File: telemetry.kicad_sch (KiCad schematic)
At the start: 52 parts, among them J1 DT13-08PA, J10 Conn_01x02, J11 Conn_01x03, J12 Conn_01x03, J13 Conn_01x03, J14 Conn_01x06, J2 Conn_01x02, J3 Conn_01x06, J4 Conn_01x06, J5 Conn_01x06, J6 Conn_01x06, J7 Conn_01x06, J8 Conn_01x06, J9 Micro_SD_Card, Q1 BS170F, Q2 BS170F, U1 RP2350_Plus, U2 MCP2517FD-xSL, U3 TLV76133DCY, U4 DS1307+, U5 R-78C5.0-1.0, U6 MCP2551-I-P, Y2 ABS07-32.768KHZ-T

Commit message: Complete (hopefully) schematic
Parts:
- removed U1: RP2350_Plus, symbol Telemetry:RP2350_Plus
- removed U2: MCP2517FD-xSL, Package_SO:SOIC-14_3.9x8.7mm_P1.27mm, symbol Interface_CAN_LIN:MCP2517FD-xSL
- added C12, C13, C14, C8, C9: 10n, Capacitor_SMD:C_0805_2012Metric, symbol Device:C_Small
- added J15, J16, J17, J18, J19: Conn_01x03, Connector_JST:JST_XA_B03B-XASK-1_1x03_P2.50mm_Vertical, symbol Connector_Generic:Conn_01x03
- added R10, R11, R12, R13, R6: 100, Resistor_SMD:R_0805_2012Metric, symbol Device:R_Small
- added U2: Waveshare ESP32-S3 Devboard, symbol Telemetry:Waveshare_ESP-S3
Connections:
- net A0_GND is gone; now on net GND: C10.2, C11.2, C5.2, J11.3 (Pin_3), J12.3 (Pin_3), J13.3 (Pin_3)
- net +3V3: now also J15.1 (Pin_1), J16.1 (Pin_1), J17.1 (Pin_1), J18.1 (Pin_1), J19.1 (Pin_1)
- net +5V: now also U2.2 (5V)
- net A0: now also U2.19 (GPIO4)
- net A0_SIG: now also J16.2 (Pin_2); no longer J13.2 (Pin_2)
- net A1: now also U2.18 (GPIO5)
- net A1_SIG: now also J17.2 (Pin_2); no longer J11.2 (Pin_2)
- net A2: now also U2.17 (GPIO6)
- net A2_SIG: now also J18.2 (Pin_2); no longer J12.2 (Pin_2)
- net GND: now also C12.2, C13.2, C14.2, C8.2, C9.2, J15.3 (Pin_3), J16.3 (Pin_3), J17.3 (Pin_3), J18.3 (Pin_3), J19.3 (Pin_3), U2.1 (GND), U2.23 (GND), U2.43 (GND), U2.44 (GND)
- net GPS(SCL/RX): now also U2.28 (GPIO42)
- net GPS(SDA/TX): now also U2.29 (GPIO41)
- net I2C0_0_GPIO: now also U2.9 (GPIO46)
- net I2C0_1_GPIO: now also U2.10 (GPIO3)
- net I2C0_SCL: now also U2.27 (GPIO2)
- net I2C0_SDA: now also U2.35 (GPIO35)
- net I2C1_0_GPIO: now also U2.37 (GPIO45)
- net I2C1_1_GPIO: now also U2.36 (GPIO0)
- net SD_CS: now also U2.8 (GPIO9)
- net SD_MISO: now also U2.12 (GPIO18)
- net SD_MOSI: now also U2.11 (GPIO8)
- net SD_SCK: now also U2.13 (GPIO17)
- net SPI1_0_CS: now also U2.32 (GPIO38)
- net SPI1_1_CS: now also U2.7 (GPIO10)
- net SPI1_MISO: now also U2.30 (GPIO40)
- net SPI1_MOSI: now also U2.33 (GPIO37)
- net SPI1_SCK: now also U2.31 (GPIO39)
- net W0: now also U2.40 (GPIO21)
- net W1: now also U2.39 (GPIO47)
- net W2: now also U2.26 (GPIO1)
- net W3: now also U2.38 (GPIO48)
- net CANRX renamed CAN_RX
- net CAN_RX: now also U2.14 (GPIO16)
- net CANTX renamed CAN_TX
- net CAN_TX: now also U2.15 (GPIO15)
- new net A3: C8.1, R6.1, U2.16 (GPIO7)
- new net A3_SIG: J19.2 (Pin_2), R6.2
- new net A4: C9.1, R10.1
- new net A4_SIG: J15.2 (Pin_2), R10.2
- new net A5: C12.1, R11.1, U2.6 (GPIO11)
- new net A5_SIG: J13.2 (Pin_2), R11.2
- new net A6: C13.1, R12.1, U2.5 (GPIO12)
- new net A6_SIG: J11.2 (Pin_2), R12.2
- new net A7: C14.1, R13.1, U2.4 (GPIO13)
- new net A7_SIG: J12.2 (Pin_2), R13.2
- new net A8: U2.3 (GPIO14)
- no-connect marks 8 -> 12
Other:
- note added: "Analogue Input Connectors"
- note added: "CAN Transeiver"
- note added: "GPS I2C/UART Connector"
- note removed: "CAN"
- note removed: "Digital Input Connectors"
- moved on the sheet: BT1, C10, C11, C5, H1, H2, H3, H4, J11, J12, J13, J14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

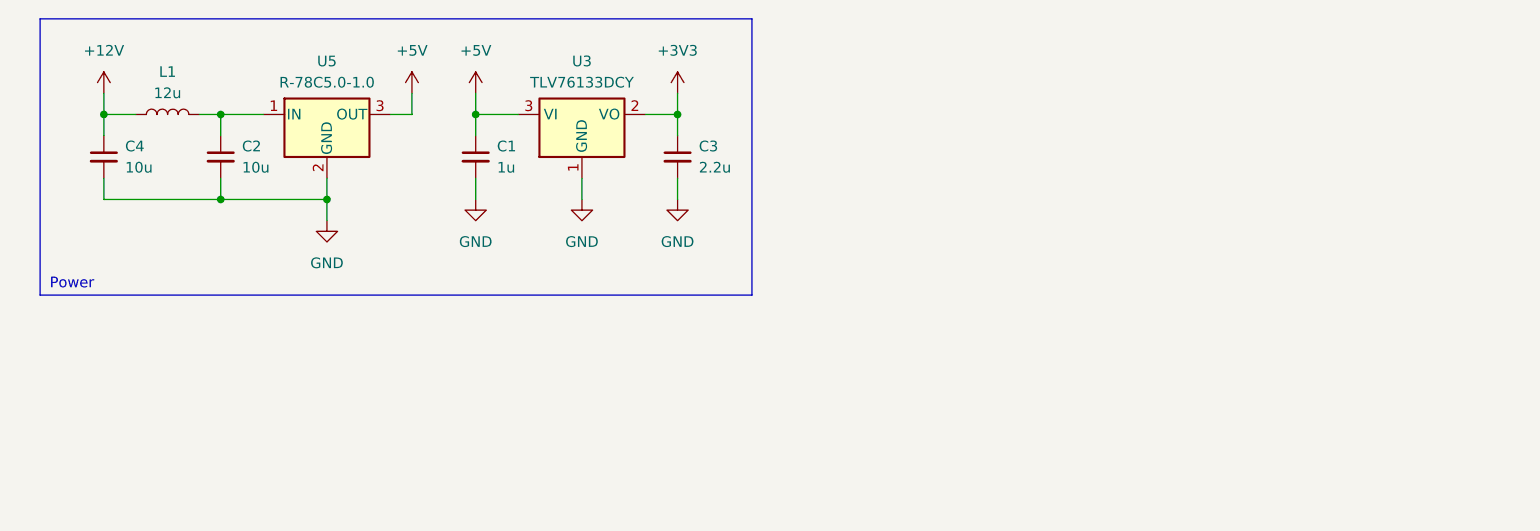
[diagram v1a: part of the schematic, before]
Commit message: added ESP32, connector footprint
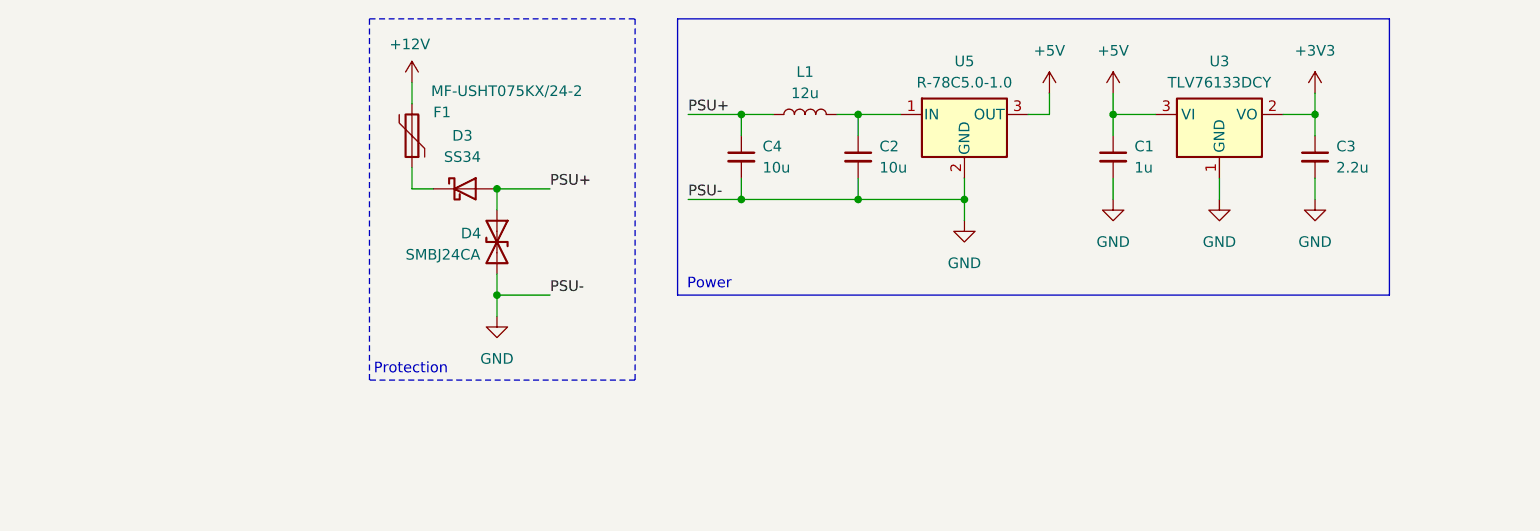
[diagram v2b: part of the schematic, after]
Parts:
- added D3: SS34, Diode_SMD:D_SMA, symbol Diode:SS34
- added D4: SMBJ24CA, Diode_SMD:D_SMB, symbol Device:D_TVS
- added F1: MF-USHT075KX/24-2, Inductor_SMD:L_1210_3225Metric, symbol Device:Polyfuse
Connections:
- net +12V: now also F1.2; no longer C4.1, L1.1
- net GND: now also D4.2 (A2)
- new net: D3.1 (K), F1.1
- new net PSU+: C4.1, D3.2 (A), D4.1 (A1), L1.1
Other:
- note added: "Protection"
- moved on the sheet: C1, C2, C3, C4, L1, U3, U5

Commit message: Place and route important components
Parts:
- removed J1: DT13-08PA, Connector_DT:TE_DT13-08PA, symbol Connector_Generic:Conn_02x04_Counter_Clockwise
- added J1, J22: Conn_01x02, Connector_JST:JST_XA_B02B-XASK-1_1x02_P2.50mm_Vertical, symbol Connector_Generic:Conn_01x02
- added J20, J21: DT13-2P, Connector_DT:TE_DT13-2P, symbol Connector_Generic:Conn_01x02
- C1, C3: footprint (none) -> Capacitor_SMD:C_0805_2012Metric
- J10, J2: value Conn_01x02 -> DT13-2P; footprint (none) -> Connector_DT:TE_DT13-2P
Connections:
- net GND: now also J1.2 (Pin_2), J20.2 (Pin_2), J21.2 (Pin_2), J22.2 (Pin_2)
- net W0: now also J1.1 (Pin_1)
- net W1: now also J22.1 (Pin_1)
- net W2: now also J20.1 (Pin_1)
- net W3: now also J21.1 (Pin_1)
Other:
- note added: "Front Wheel Speed Sensors"
- note added: "Power Supply"
- note added: "Rear Wheel Speed Sensors"
- note removed: "Power"
- note removed: "Wheel Speed Sensors Connector"
- moved on the sheet: C1, C2, C3, C4, D3, D4, F1, H1, H2, H3, H4, J10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

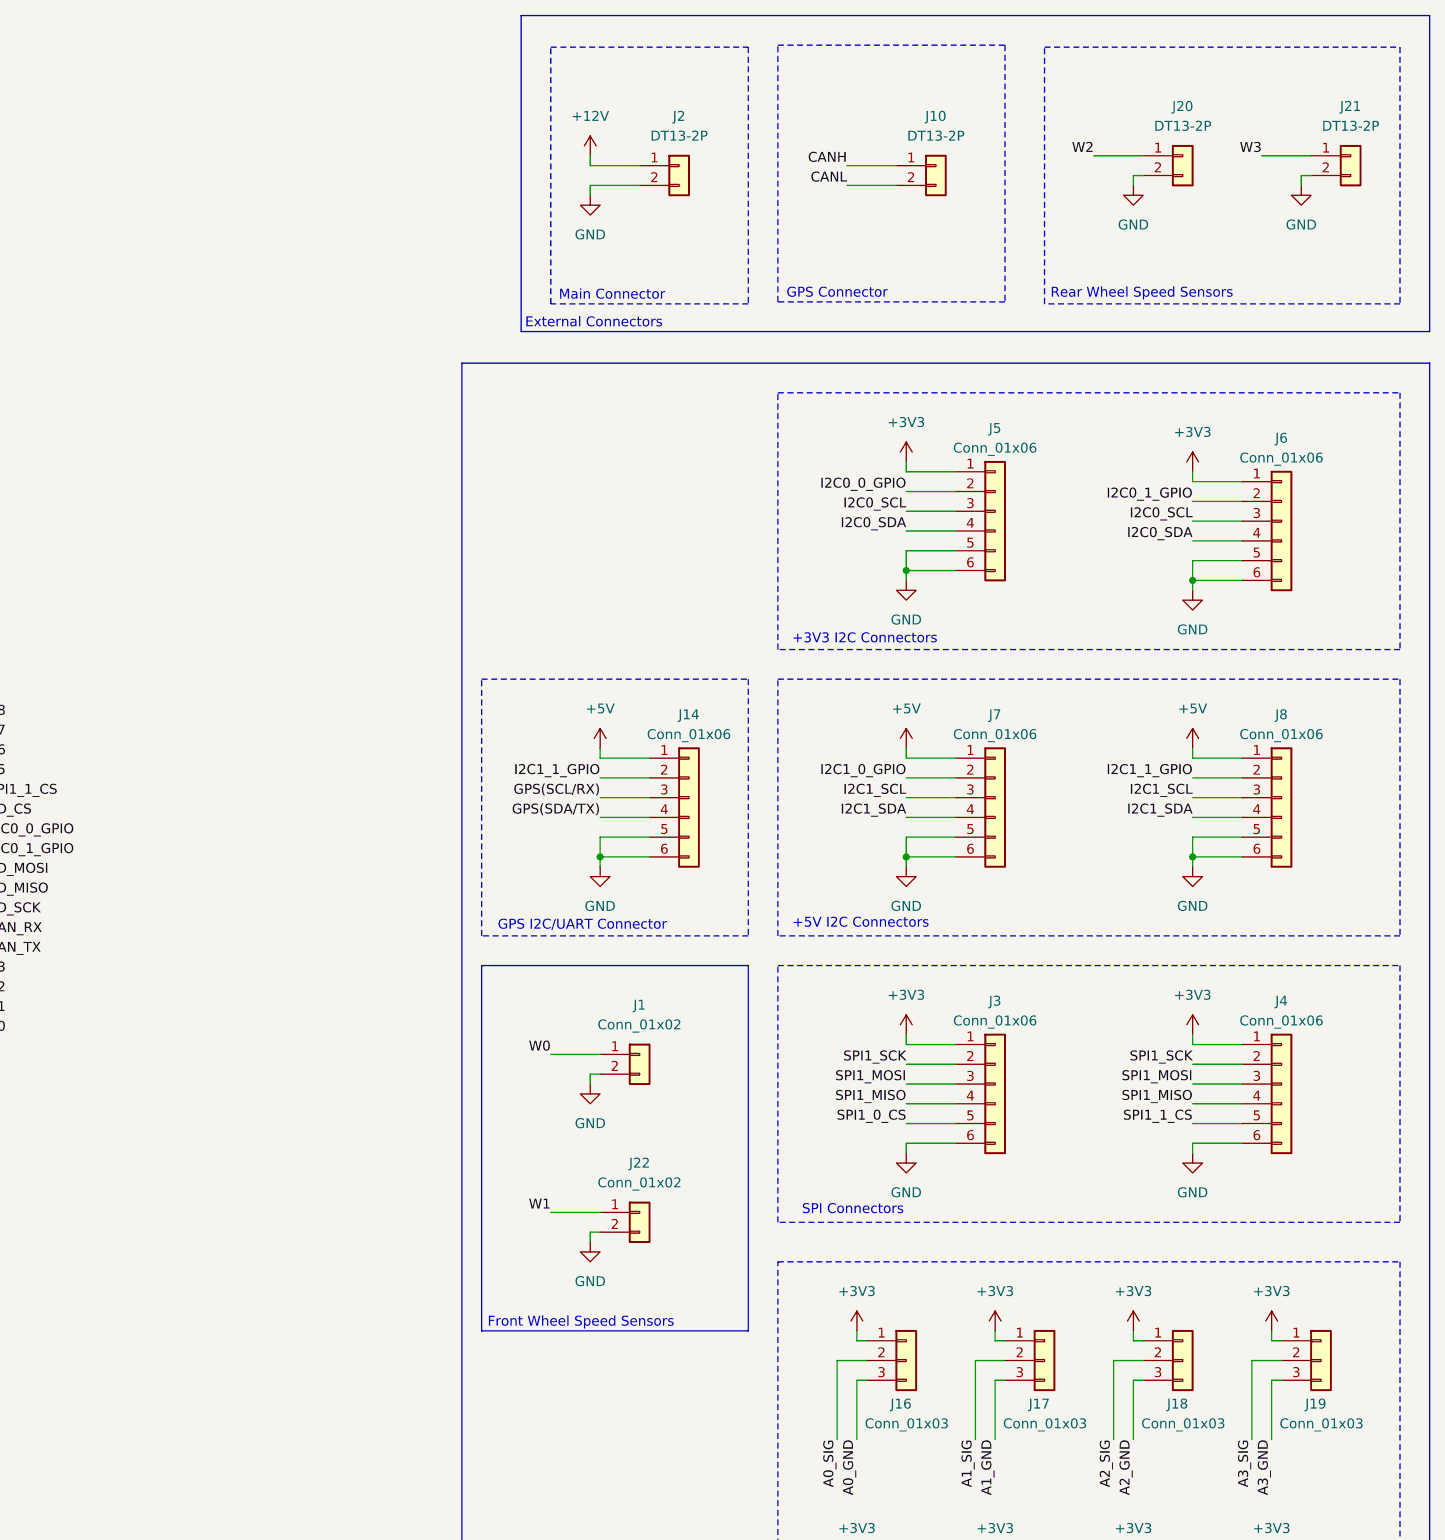
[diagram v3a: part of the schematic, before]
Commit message: Add +3V3 pin to internal WSS connectors
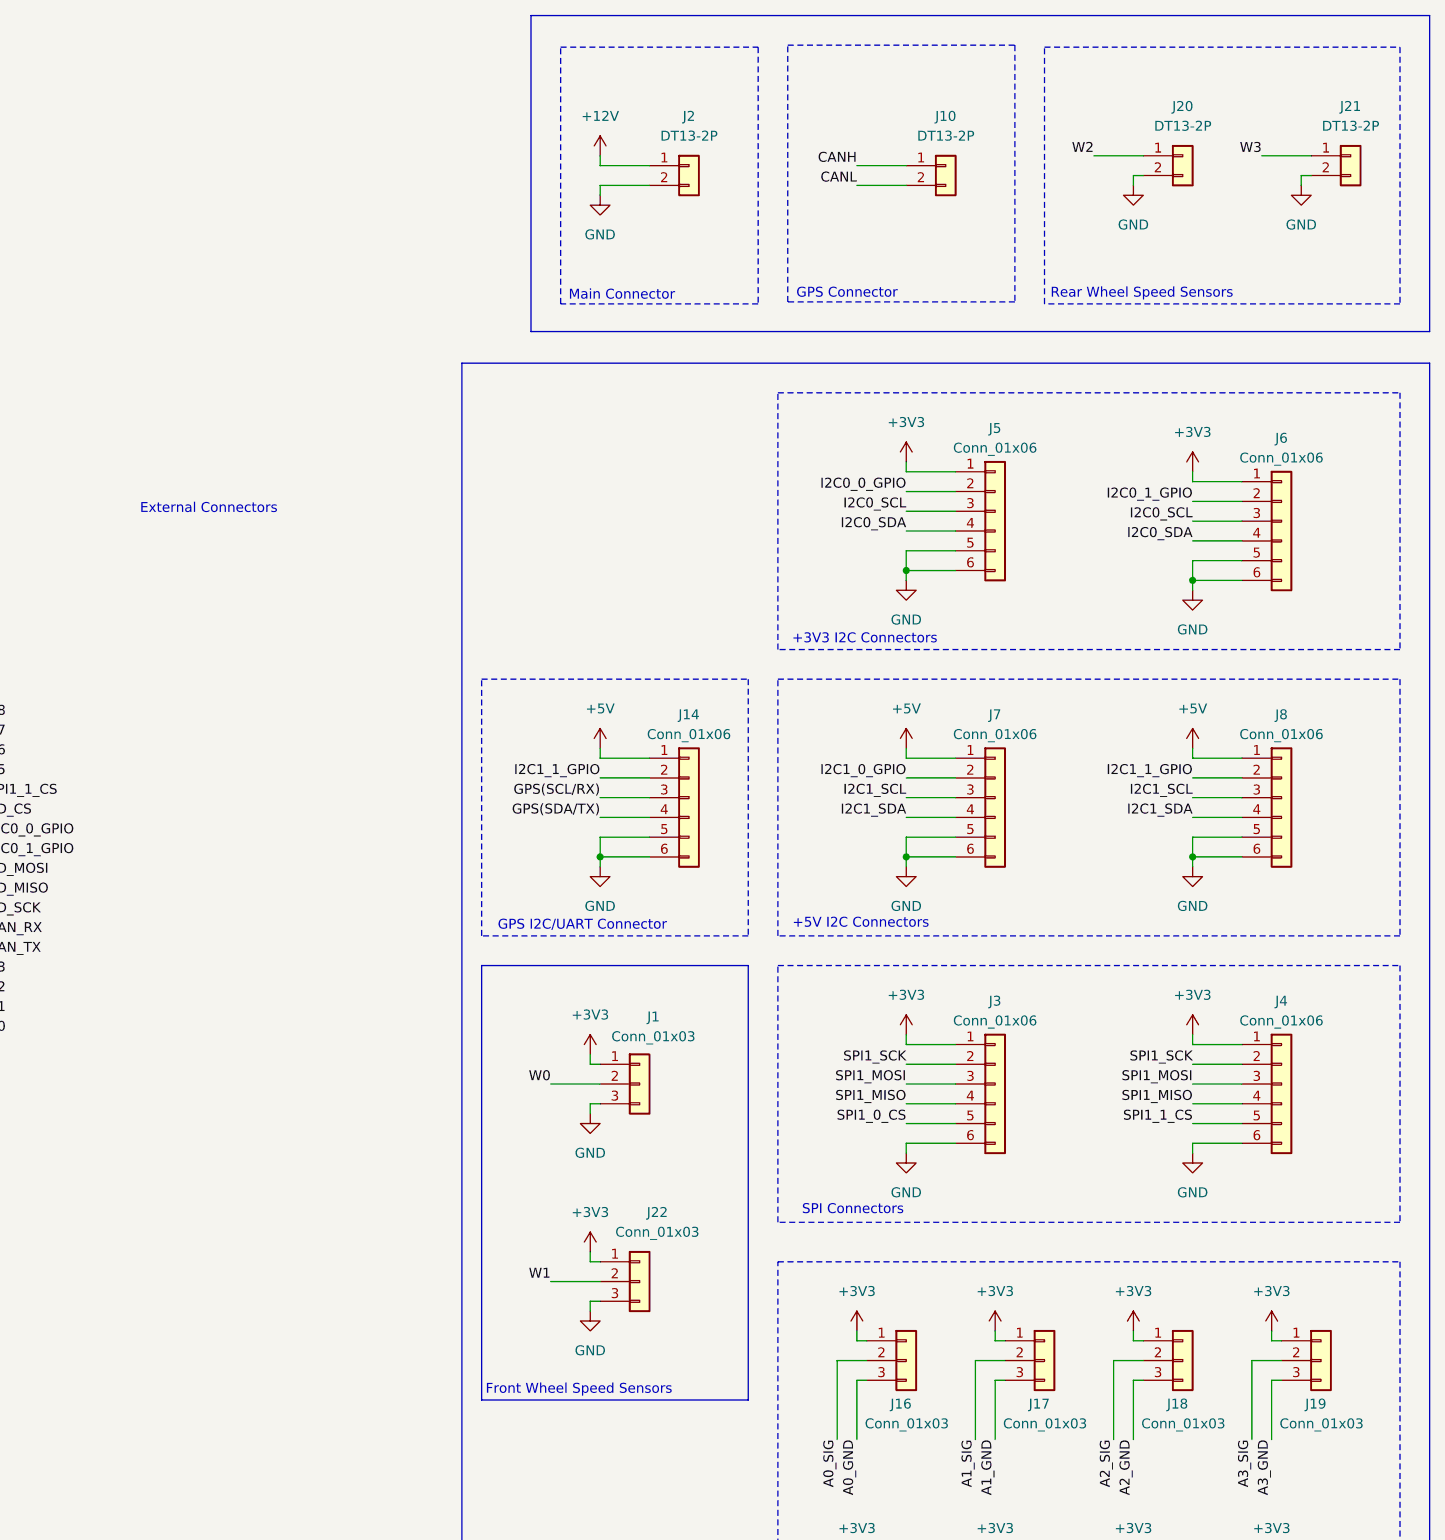
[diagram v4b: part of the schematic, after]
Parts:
- removed J1, J22: Conn_01x02, Connector_JST:JST_XA_B02B-XASK-1_1x02_P2.50mm_Vertical, symbol Connector_Generic:Conn_01x02
- added J1, J22: Conn_01x03, Connector_JST:JST_XA_B03B-XASK-1_1x03_P2.50mm_Vertical, symbol Connector_Generic:Conn_01x03
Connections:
- net +3V3: now also J1.1 (Pin_1), J22.1 (Pin_1)
- net GND: now also J1.3 (Pin_3), J22.3 (Pin_3)
- net W0: now also J1.2 (Pin_2)
- net W1: now also J22.2 (Pin_2)
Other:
- moved on the sheet: J10, J2

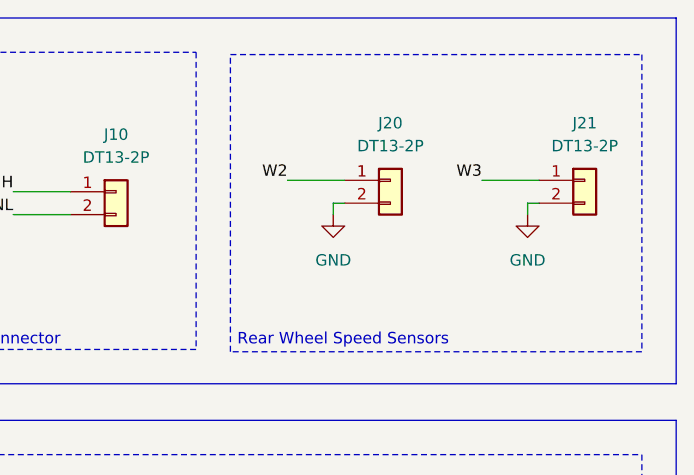
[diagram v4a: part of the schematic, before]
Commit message: Switch to SIG+3V3 for Back WSS
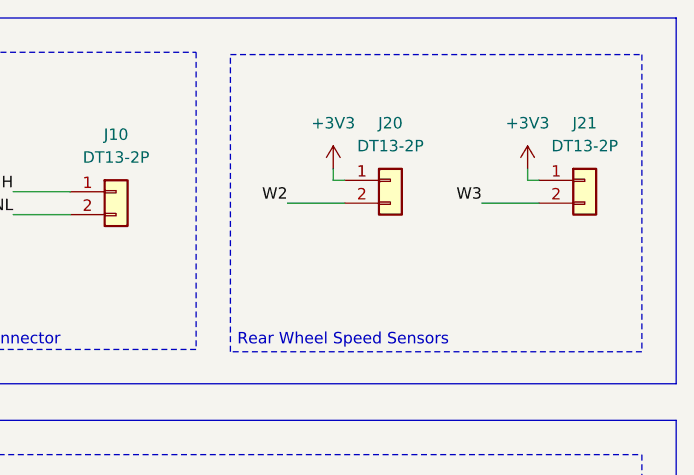
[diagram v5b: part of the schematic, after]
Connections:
- net +3V3: now also J20.1 (Pin_1), J21.1 (Pin_1)
- net GND: no longer J20.2 (Pin_2), J21.2 (Pin_2)
- net W2: now also J20.2 (Pin_2); no longer J20.1 (Pin_1)
- net W3: now also J21.2 (Pin_2); no longer J21.1 (Pin_1)

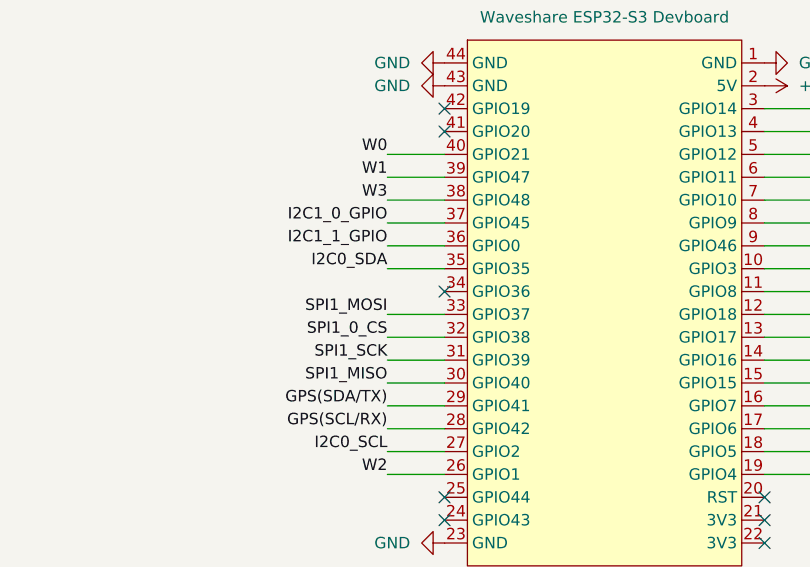
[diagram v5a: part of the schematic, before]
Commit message: Arranged remaining components, added few tracks
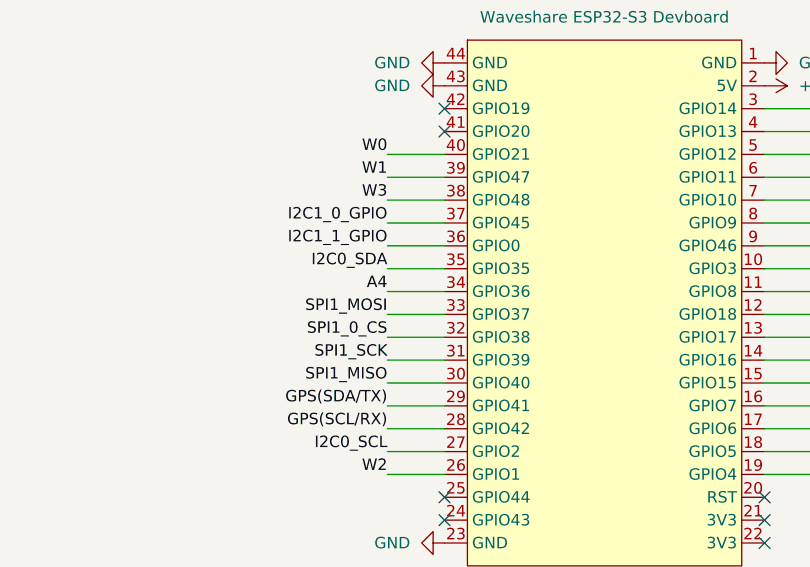
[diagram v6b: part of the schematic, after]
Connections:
- net A4: now also U2.34 (GPIO36)
- no-connect marks 12 -> 11
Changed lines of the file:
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@@
 	)
 	(no_connect
-		(at 175.26 128.27)
-	)
-	(no_connect
 		(at 210.82 151.13)
 	)
@@
 	(wire
 		(pts
+			(xy 168.91 128.27) (xy 175.26 128.27)
+		)
+		(stroke
+			(width 0)
+			(type default)
+		)
+	)
+	(wire
+		(pts
 			(xy 217.17 110.49) (xy 210.82 110.49)
 		)
@@
 		(effects
 			(font
+				(size 1.27 1.27)
+			)
+			(justify right bottom)
+		)
+	)
+	(label "A4"
+		(at 168.91 128.27 180)
+		(effects
+			(font

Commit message: Slim board
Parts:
- removed J2, J20, J21: DT13-2P, Connector_DT:TE_DT13-2P, symbol Connector_Generic:Conn_01x02
- added J23: DT13-08PA, Connector_DT:TE_DT13-08PA, symbol Connector_Generic:Conn_02x04_Odd_Even
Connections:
- net +12V: now also J23.1 (Pin_1)
- net +3V3: now also J23.3 (Pin_3), J23.5 (Pin_5)
- net GND: now also J23.2 (Pin_2), J23.7 (Pin_7), J23.8 (Pin_8)
- net W2: now also J23.4 (Pin_4)
- net W3: now also J23.6 (Pin_6)
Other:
- note added: "CAN Connector"
- note added: "Car"
- note removed: "GPS Connector"
- note removed: "Main Connector"
- note removed: "Rear Wheel Speed Sensors"
- moved on the sheet: J10
